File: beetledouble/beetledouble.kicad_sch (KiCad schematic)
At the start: 27 parts, among them J1 power in, J2 rxin, J6 prog connector, U1 78L12G-AB3-R, U2 DD4012SB, U3 ATtiny1614-SS

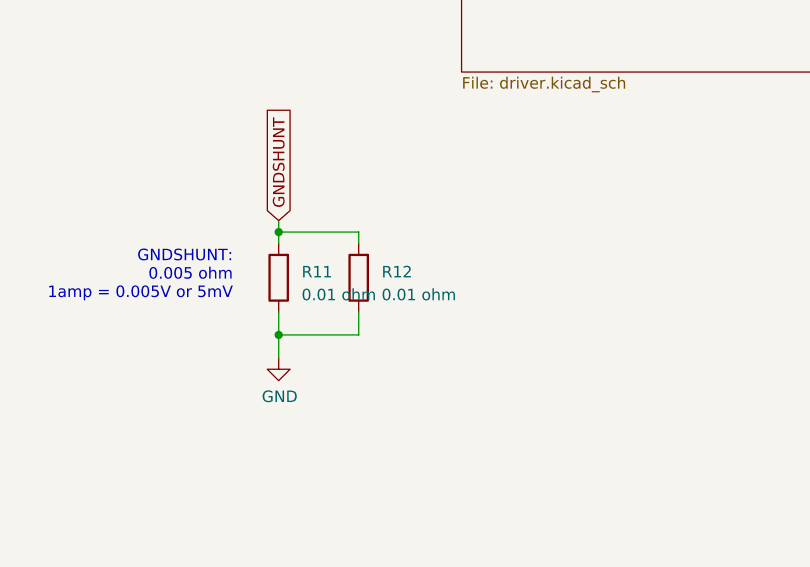
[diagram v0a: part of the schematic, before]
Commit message: Beetle double driver update with differen fets
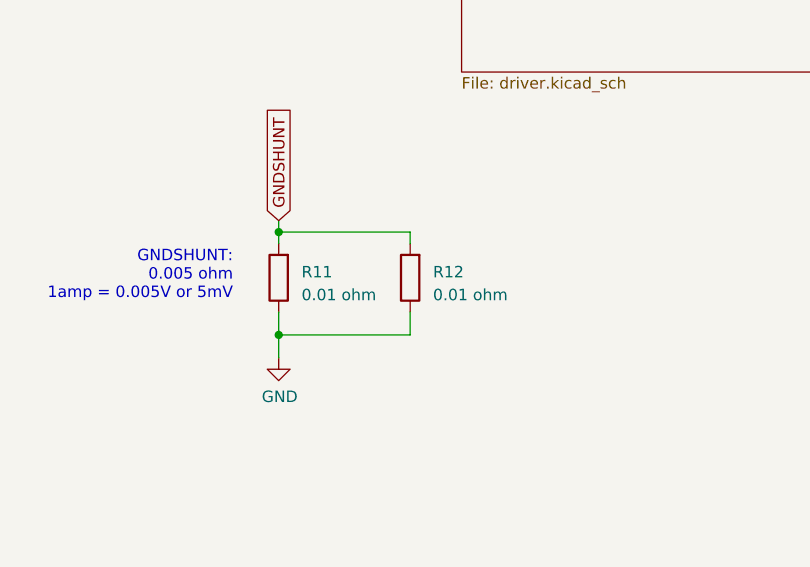
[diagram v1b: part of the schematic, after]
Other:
- moved on the sheet: R12
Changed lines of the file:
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@@
     (stroke (width 0) (type solid) (color 0 0 0 0))
   )
-  (wire (pts (xy 195.58 138.43) (xy 204.47 138.43))
+  (wire (pts (xy 195.58 138.43) (xy 210.185 138.43))
     (stroke (width 0) (type solid) (color 0 0 0 0))
   )
@@
     (stroke (width 0) (type solid) (color 0 0 0 0))
   )
-  (wire (pts (xy 204.47 138.43) (xy 204.47 139.7))
-    (stroke (width 0) (type solid) (color 0 0 0 0))
-  )
-  (wire (pts (xy 204.47 147.32) (xy 204.47 149.86))
-    (stroke (width 0) (type solid) (color 0 0 0 0))
-  )
-  (wire (pts (xy 204.47 149.86) (xy 195.58 149.86))
+  (wire (pts (xy 210.185 138.43) (xy 210.185 139.7))
+    (stroke (width 0) (type solid) (color 0 0 0 0))
+  )
+  (wire (pts (xy 210.185 147.32) (xy 210.185 149.86))
+    (stroke (width 0) (type solid) (color 0 0 0 0))
+  )
+  (wire (pts (xy 210.185 149.86) (xy 195.58 149.86))
     (stroke (width 0) (type solid) (color 0 0 0 0))
   )
@@
     (pin "2")
   )
-  (symbol (lib_id "Device:R") (at 204.47 143.51 180) (unit 1)
-    (in_bom yes) (on_board yes) (fields_autoplaced)
-    (property "Reference" "R12" (id 0) (at 207.01 142.8749 0)
+  (symbol (lib_id "Device:R") (at 210.185 143.51 180) (unit 1)
+    (in_bom yes) (on_board yes) (fields_autoplaced)
+    (property "Reference" "R12" (id 0) (at 212.725 142.8749 0)
       (effects (font (size 1.27 1.27)) (justify right))
     )
-    (property "Value" "0.01 ohm" (id 1) (at 207.01 145.4149 0)
+    (property "Value" "0.01 ohm" (id 1) (at 212.725 145.4149 0)
       (effects (font (size 1.27 1.27)) (justify right))
     )
-    (property "Footprint" "Resistor_SMD:R_2512_6332Metric_Pad1.40x3.35mm_HandSolder" (id 2) (at 206.248 143.51 90)
-      (effects (font (size 1.27 1.27)) hide)
-    )
-    (property "Datasheet" "~" (id 3) (at 204.47 143.51 0)
+    (property "Footprint" "Resistor_SMD:R_2512_6332Metric_Pad1.40x3.35mm_HandSolder" (id 2) (at 211.963 143.51 90)
+      (effects (font (size 1.27 1.27)) hide)
+    )
+    (property "Datasheet" "~" (id 3) (at 210.185 143.51 0)
       (effects (font (size 1.27 1.27)) hide)
     )
@@
       (reference "J4") (unit 1) (value "motor_out") (footprint "Connector_Wire:SolderWire-0.75sqmm_1x02_P4.8mm_D1.25mm_OD2.3mm")
     )
-    (path "/04625774-148a-4b57-bc94-9367edc01ebb/b1a06d2a-a007-41d4-9e0c-37fd31a792da"
-      (reference "Q1") (unit 1) (value "IRF8313PBF ") (footprint "Package_SO:SOIC-8_3.9x4.9mm_P1.27mm")
-    )
-    (path "/04625774-148a-4b57-bc94-9367edc01ebb/453e55ff-63c7-4e45-b1a7-07e090e6dab9"
-      (reference "Q1") (unit 2) (value "IRF8313PBF ") (footprint "Package_SO:SOIC-8_3.9x4.9mm_P1.27mm")
-    )
-    (path "/04625774-148a-4b57-bc94-9367edc01ebb/3e33f540-466e-4b3e-a64f-d1be0667f819"
-      (reference "Q2") (unit 1) (value "IRF8313PBF ") (footprint "Package_SO:SOIC-8_3.9x4.9mm_P1.27mm")
-    )
-    (path "/04625774-148a-4b57-bc94-9367edc01ebb/f58403f9-1add-43f1-814c-ff493d5d1e52"
-      (reference "Q2") (unit 2) (value "IRF8313PBF ") (footprint "Package_SO:SOIC-8_3.9x4.9mm_P1.27mm")
+    (path "/04625774-148a-4b57-bc94-9367edc01ebb/91401f80-e11e-4dcd-8127-cf1209ae9c95"
+      (reference "Q1") (unit 1) (value "IPG20N04S4-12") (footprint "beetledouble:Infineon-PG-TDSON")
+    )
+    (path "/04625774-148a-4b57-bc94-9367edc01ebb/78f7d384-c1e8-43be-9cf5-ea0b8e5ee852"
+      (reference "Q1") (unit 2) (value "IPG20N04S4-12") (footprint "beetledouble:Infineon-PG-TDSON")
+    )
+    (path "/04625774-148a-4b57-bc94-9367edc01ebb/e735ae3b-e647-4157-bf24-522fcab1aa8b"
+      (reference "Q2") (unit 1) (value "IPG20N04S4-12") (footprint "beetledouble:Infineon-PG-TDSON")
+    )
+    (path "/04625774-148a-4b57-bc94-9367edc01ebb/a45d94ed-e4aa-467a-8892-f6d35332ba60"
+      (reference "Q2") (unit 2) (value "IPG20N04S4-12") (footprint "beetledouble:Infineon-PG-TDSON")
     )
     (path "/04625774-148a-4b57-bc94-9367edc01ebb/fad7411d-71dd-41a2-9e10-172d90ee0b89"
@@
       (reference "J5") (unit 1) (value "motor_out") (footprint "Connector_Wire:SolderWire-0.75sqmm_1x02_P4.8mm_D1.25mm_OD2.3mm")
     )
-    (path "/4bcd2397-838c-4768-a766-b8196d1dcd9f/b1a06d2a-a007-41d4-9e0c-37fd31a792da"
-      (reference "Q3") (unit 1) (value "IRF8313PBF ") (footprint "Package_SO:SOIC-8_3.9x4.9mm_P1.27mm")
-    )
-    (path "/4bcd2397-838c-4768-a766-b8196d1dcd9f/453e55ff-63c7-4e45-b1a7-07e090e6dab9"
-      (reference "Q3") (unit 2) (value "IRF8313PBF ") (footprint "Package_SO:SOIC-8_3.9x4.9mm_P1.27mm")
-    )
-    (path "/4bcd2397-838c-4768-a766-b8196d1dcd9f/3e33f540-466e-4b3e-a64f-d1be0667f819"
-      (reference "Q4") (unit 1) (value "IRF8313PBF ") (footprint "Package_SO:SOIC-8_3.9x4.9mm_P1.27mm")
-    )
-    (path "/4bcd2397-838c-4768-a766-b8196d1dcd9f/f58403f9-1add-43f1-814c-ff493d5d1e52"
-      (reference "Q4") (unit 2) (value "IRF8313PBF ") (footprint "Package_SO:SOIC-8_3.9x4.9mm_P1.27mm")
+    (path "/4bcd2397-838c-4768-a766-b8196d1dcd9f/91401f80-e11e-4dcd-8127-cf1209ae9c95"
+      (reference "Q3") (unit 1) (value "IPG20N04S4-12") (footprint "beetledouble:Infineon-PG-TDSON")
+    )
+    (path "/4bcd2397-838c-4768-a766-b8196d1dcd9f/78f7d384-c1e8-43be-9cf5-ea0b8e5ee852"
+      (reference "Q3") (unit 2) (value "IPG20N04S4-12") (footprint "beetledouble:Infineon-PG-TDSON")
+    )
+    (path "/4bcd2397-838c-4768-a766-b8196d1dcd9f/e735ae3b-e647-4157-bf24-522fcab1aa8b"
+      (reference "Q4") (unit 1) (value "IPG20N04S4-12") (footprint "beetledouble:Infineon-PG-TDSON")
+    )
+    (path "/4bcd2397-838c-4768-a766-b8196d1dcd9f/a45d94ed-e4aa-467a-8892-f6d35332ba60"
+      (reference "Q4") (unit 2) (value "IPG20N04S4-12") (footprint "beetledouble:Infineon-PG-TDSON")
     )
     (path "/4bcd2397-838c-4768-a766-b8196d1dcd9f/fad7411d-71dd-41a2-9e10-172d90ee0b89"

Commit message: beetledouble esc wip
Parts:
- added C10: 2.2uF, Capacitor_SMD:C_0603_1608Metric, symbol Device:C
- J1: value power in -> XT30PW-M
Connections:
- net GND: now also C10.2
- net ISENSE: now also C10.1
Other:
- moved on the sheet: R13
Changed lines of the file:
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@@
   (junction (at 71.755 99.695) (diameter 0.9144) (color 0 0 0 0))
   (junction (at 76.835 99.695) (diameter 0.9144) (color 0 0 0 0))
+  (junction (at 119.38 78.74) (diameter 0.9144) (color 0 0 0 0))
   (junction (at 137.16 189.23) (diameter 0.9144) (color 0 0 0 0))
   (junction (at 152.4 60.96) (diameter 0.9144) (color 0 0 0 0))
@@
     (stroke (width 0) (type solid) (color 0 0 0 0))
   )
-  (wire (pts (xy 120.65 78.74) (xy 120.65 81.28))
+  (wire (pts (xy 111.76 78.74) (xy 119.38 78.74))
+    (stroke (width 0) (type solid) (color 0 0 0 0))
+  )
+  (wire (pts (xy 119.38 78.74) (xy 119.38 83.82))
+    (stroke (width 0) (type solid) (color 0 0 0 0))
+  )
+  (wire (pts (xy 119.38 78.74) (xy 137.16 78.74))
     (stroke (width 0) (type solid) (color 0 0 0 0))
   )
@@
   )
   (wire (pts (xy 134.62 60.96) (xy 152.4 60.96))
-    (stroke (width 0) (type solid) (color 0 0 0 0))
-  )
-  (wire (pts (xy 137.16 78.74) (xy 120.65 78.74))
     (stroke (width 0) (type solid) (color 0 0 0 0))
   )
@@
     )
   )
-  (global_label "GNDSHUNT" (shape input) (at 120.65 88.9 270)
+  (global_label "GNDSHUNT" (shape input) (at 111.76 86.36 270)
     (effects (font (size 1.27 1.27)) (justify right))
-    (property "Intersheet References" "${INTERSHEET_REFS}" (id 0) (at 120.5706 102.8761 90)
+    (property "Intersheet References" "${INTERSHEET_REFS}" (id 0) (at 111.6806 100.3361 90)
       (effects (font (size 1.27 1.27)) (justify right) hide)
     )
@@
     (pin "1")
   )
+  (symbol (lib_id "power:GND") (at 119.38 91.44 0) (unit 1)
+    (in_bom yes) (on_board yes)
+    (property "Reference" "#PWR0102" (id 0) (at 119.38 97.79 0)
+      (effects (font (size 1.27 1.27)) hide)
+    )
+    (property "Value" "GND" (id 1) (at 119.4943 95.7644 0))
+    (property "Footprint" "" (id 2) (at 119.38 91.44 0)
+      (effects (font (size 1.27 1.27)) hide)
+    )
+    (property "Datasheet" "" (id 3) (at 119.38 91.44 0)
+      (effects (font (size 1.27 1.27)) hide)
+    )
+    (pin "1")
+  )
   (symbol (lib_id "power:GND") (at 134.62 68.58 0) (unit 1)
     (in_bom yes) (on_board yes)
@@
     (pin "2")
   )
-  (symbol (lib_id "Device:R") (at 120.65 85.09 180) (unit 1)
-    (in_bom yes) (on_board yes)
-    (property "Reference" "R13" (id 0) (at 115.4238 85.09 90))
-    (property "Value" "1k" (id 1) (at 117.7225 85.09 90))
-    (property "Footprint" "Resistor_SMD:R_0603_1608Metric" (id 2) (at 122.428 85.09 90)
-      (effects (font (size 1.27 1.27)) hide)
-    )
-    (property "Datasheet" "~" (id 3) (at 120.65 85.09 0)
+  (symbol (lib_id "Device:R") (at 111.76 82.55 180) (unit 1)
+    (in_bom yes) (on_board yes)
+    (property "Reference" "R13" (id 0) (at 106.5338 82.55 90))
+    (property "Value" "1k" (id 1) (at 108.8325 82.55 90))
+    (property "Footprint" "Resistor_SMD:R_0603_1608Metric" (id 2) (at 113.538 82.55 90)
+      (effects (font (size 1.27 1.27)) hide)
+    )
+    (property "Datasheet" "~" (id 3) (at 111.76 82.55 0)
       (effects (font (size 1.27 1.27)) hide)
     )
@@
     (in_bom yes) (on_board yes)
     (property "Reference" "J1" (id 0) (at 25.5524 55.88 0))
-    (property "Value" "power in" (id 1) (at 24.2824 53.34 0))
+    (property "Value" "XT30PW-M" (id 1) (at 24.2824 53.34 0))
     (property "Footprint" "beetledouble:beetlepower" (id 2) (at 22.86 62.23 0)
       (effects (font (size 1.27 1.27)) hide)
@@
     )
     (property "LCSC" "C50254" (id 4) (at 71.755 103.505 0)
+      (effects (font (size 1.27 1.27)) hide)
+    )
+    (pin "1")
+    (pin "2")
+  )
+  (symbol (lib_id "Device:C") (at 119.38 87.63 0) (unit 1)
+    (in_bom yes) (on_board yes)
+    (property "Reference" "C10" (id 0) (at 122.301 86.481 0)
+      (effects (font (size 1.27 1.27)) (justify left))
+    )
+    (property "Value" "2.2uF" (id 1) (at 122.3011 88.7793 0)
+      (effects (font (size 1.27 1.27)) (justify left))
+    )
+    (property "Footprint" "Capacitor_SMD:C_0603_1608Metric" (id 2) (at 120.3452 91.44 0)
+      (effects (font (size 1.27 1.27)) hide)
+    )
+    (property "Datasheet" "~" (id 3) (at 119.38 87.63 0)
+      (effects (font (size 1.27 1.27)) hide)
+    )
+    (property "LCSC" "" (id 4) (at 119.38 87.63 0)
       (effects (font (size 1.27 1.27)) hide)
     )
@@
       (reference "#PWR0101") (unit 1) (value "GND") (footprint "")
     )
+    (path "/3a8b150a-c300-43cd-8e05-40b55ad8dd46"
+      (reference "#PWR0102") (unit 1) (value "GND") (footprint "")
+    )
     (path "/3d5e6458-1bc6-4cb1-8b72-23ca99e73989"
       (reference "#PWR0103") (unit 1) (value "+5V") (footprint "")
@@
       (reference "C9") (unit 1) (value "0.1uF") (footprint "Capacitor_SMD:C_0603_1608Metric")
     )
+    (path "/ec931dfe-fcd6-43aa-a942-f11aa5bf6441"
+      (reference "C10") (unit 1) (value "2.2uF") (footprint "Capacitor_SMD:C_0603_1608Metric")
+    )
     (path "/c473e51e-eda3-4e25-b100-c0ce34b1e3be"
       (reference "D1") (unit 1) (value "LED") (footprint "LED_SMD:LED_0603_1608Metric_Pad1.05x0.95mm_HandSolder")
@@
     )
     (path "/b70e717b-9e3e-42dc-96e9-65039080dd01"
-      (reference "J1") (unit 1) (value "power in") (footprint "beetledouble:beetlepower")
+      (reference "J1") (unit 1) (value "XT30PW-M") (footprint "beetledouble:beetlepower")
     )
     (path "/259582c8-52ac-48ed-9e5f-c74948d79057"

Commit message: Beetle esc
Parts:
- C10: value 2.2uF -> 2.2uF 50V; LCSC (none) -> C50254
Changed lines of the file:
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@@
       (effects (font (size 1.27 1.27)) (justify left))
     )
-    (property "Value" "2.2uF" (id 1) (at 122.3011 88.7793 0)
+    (property "Value" "2.2uF 50V" (id 1) (at 122.3011 88.7793 0)
       (effects (font (size 1.27 1.27)) (justify left))
     )
@@
       (effects (font (size 1.27 1.27)) hide)
     )
-    (property "LCSC" "" (id 4) (at 119.38 87.63 0)
+    (property "LCSC" "C50254" (id 4) (at 119.38 87.63 0)
       (effects (font (size 1.27 1.27)) hide)
     )
@@
     )
     (path "/ec931dfe-fcd6-43aa-a942-f11aa5bf6441"
-      (reference "C10") (unit 1) (value "2.2uF") (footprint "Capacitor_SMD:C_0603_1608Metric")
+      (reference "C10") (unit 1) (value "2.2uF 50V") (footprint "Capacitor_SMD:C_0603_1608Metric")
     )
     (path "/c473e51e-eda3-4e25-b100-c0ce34b1e3be"
@@
       (reference "#PWR09") (unit 1) (value "GND") (footprint "")
     )
+    (path "/04625774-148a-4b57-bc94-9367edc01ebb/349a753b-3547-4ca7-ac39-04fbb7832ae1"
+      (reference "C3") (unit 1) (value "2.2uF 50V") (footprint "Capacitor_SMD:C_0603_1608Metric")
+    )
     (path "/04625774-148a-4b57-bc94-9367edc01ebb/88333258-cec2-4c47-95fd-16fbcefc9469"
-      (reference "C3") (unit 1) (value "2.2uF 50V") (footprint "Capacitor_SMD:C_0603_1608Metric")
-    )
-    (path "/04625774-148a-4b57-bc94-9367edc01ebb/349a753b-3547-4ca7-ac39-04fbb7832ae1"
       (reference "C4") (unit 1) (value "2.2uF 50V") (footprint "Capacitor_SMD:C_0603_1608Metric")
+    )
+    (path "/04625774-148a-4b57-bc94-9367edc01ebb/e0439b6c-59c5-4831-b158-7336fb8aeef6"
+      (reference "D3") (unit 1) (value "B5819W") (footprint "Diode_SMD:D_SOD-123")
+    )
+    (path "/04625774-148a-4b57-bc94-9367edc01ebb/e793d2f4-d15d-4c68-aa28-2d98997ea5fe"
+      (reference "D4") (unit 1) (value "B5819W") (footprint "Diode_SMD:D_SOD-123")
     )
     (path "/04625774-148a-4b57-bc94-9367edc01ebb/8550bf63-6bc2-479c-bddc-082389ddbc28"
@@
     )
     (path "/04625774-148a-4b57-bc94-9367edc01ebb/91401f80-e11e-4dcd-8127-cf1209ae9c95"
-      (reference "Q1") (unit 1) (value "IPG20N04S4-12") (footprint "beetledouble:Infineon-PG-TDSON")
+      (reference "Q1") (unit 1) (value "AON6884") (footprint "beetledouble:Infineon-PG-TDSON")
     )
     (path "/04625774-148a-4b57-bc94-9367edc01ebb/78f7d384-c1e8-43be-9cf5-ea0b8e5ee852"
-      (reference "Q1") (unit 2) (value "IPG20N04S4-12") (footprint "beetledouble:Infineon-PG-TDSON")
+      (reference "Q1") (unit 2) (value "AON6884") (footprint "beetledouble:Infineon-PG-TDSON")
     )
     (path "/04625774-148a-4b57-bc94-9367edc01ebb/e735ae3b-e647-4157-bf24-522fcab1aa8b"
-      (reference "Q2") (unit 1) (value "IPG20N04S4-12") (footprint "beetledouble:Infineon-PG-TDSON")
+      (reference "Q2") (unit 1) (value "AON6884") (footprint "beetledouble:Infineon-PG-TDSON")
     )
     (path "/04625774-148a-4b57-bc94-9367edc01ebb/a45d94ed-e4aa-467a-8892-f6d35332ba60"
-      (reference "Q2") (unit 2) (value "IPG20N04S4-12") (footprint "beetledouble:Infineon-PG-TDSON")
+      (reference "Q2") (unit 2) (value "AON6884") (footprint "beetledouble:Infineon-PG-TDSON")
     )
     (path "/04625774-148a-4b57-bc94-9367edc01ebb/fad7411d-71dd-41a2-9e10-172d90ee0b89"
@@
       (reference "R4") (unit 1) (value "10R") (footprint "Resistor_SMD:R_0603_1608Metric")
     )
-    (path "/04625774-148a-4b57-bc94-9367edc01ebb/95483e26-d500-422a-bbff-b6400f3d51be"
-      (reference "U4") (unit 1) (value "NCP81155MNTXG") (footprint "beetledouble:DFN-8-3x3mm_hand1")
-    )
-    (path "/04625774-148a-4b57-bc94-9367edc01ebb/7e2cc32c-9391-4594-89cf-8d65ae70b10c"
-      (reference "U5") (unit 1) (value "NCP81155MNTXG") (footprint "beetledouble:DFN-8-3x3mm_hand1")
+    (path "/04625774-148a-4b57-bc94-9367edc01ebb/074b7fbd-db44-4cf2-a152-10215821aa61"
+      (reference "U4") (unit 1) (value "ADP3110A") (footprint "beetledouble:DFN-8-3x3mm_hand1")
+    )
+    (path "/04625774-148a-4b57-bc94-9367edc01ebb/9ede5968-a869-4148-88dc-1a510a7e3341"
+      (reference "U5") (unit 1) (value "ADP3110A") (footprint "beetledouble:DFN-8-3x3mm_hand1")
     )
     (path "/4bcd2397-838c-4768-a766-b8196d1dcd9f/5beb08dd-33fb-4b19-bec1-9311e4c1305f"
@@
       (reference "#PWR013") (unit 1) (value "GND") (footprint "")
     )
+    (path "/4bcd2397-838c-4768-a766-b8196d1dcd9f/349a753b-3547-4ca7-ac39-04fbb7832ae1"
+      (reference "C5") (unit 1) (value "2.2uF 50V") (footprint "Capacitor_SMD:C_0603_1608Metric")
+    )
     (path "/4bcd2397-838c-4768-a766-b8196d1dcd9f/88333258-cec2-4c47-95fd-16fbcefc9469"
-      (reference "C5") (unit 1) (value "2.2uF 50V") (footprint "Capacitor_SMD:C_0603_1608Metric")
-    )
-    (path "/4bcd2397-838c-4768-a766-b8196d1dcd9f/349a753b-3547-4ca7-ac39-04fbb7832ae1"
       (reference "C6") (unit 1) (value "2.2uF 50V") (footprint "Capacitor_SMD:C_0603_1608Metric")
+    )
+    (path "/4bcd2397-838c-4768-a766-b8196d1dcd9f/e0439b6c-59c5-4831-b158-7336fb8aeef6"
+      (reference "D5") (unit 1) (value "B5819W") (footprint "Diode_SMD:D_SOD-123")
+    )
+    (path "/4bcd2397-838c-4768-a766-b8196d1dcd9f/e793d2f4-d15d-4c68-aa28-2d98997ea5fe"
+      (reference "D6") (unit 1) (value "B5819W") (footprint "Diode_SMD:D_SOD-123")
     )
     (path "/4bcd2397-838c-4768-a766-b8196d1dcd9f/8550bf63-6bc2-479c-bddc-082389ddbc28"
@@
     )
     (path "/4bcd2397-838c-4768-a766-b8196d1dcd9f/91401f80-e11e-4dcd-8127-cf1209ae9c95"
-      (reference "Q3") (unit 1) (value "IPG20N04S4-12") (footprint "beetledouble:Infineon-PG-TDSON")
+      (reference "Q3") (unit 1) (value "AON6884") (footprint "beetledouble:Infineon-PG-TDSON")
     )
     (path "/4bcd2397-838c-4768-a766-b8196d1dcd9f/78f7d384-c1e8-43be-9cf5-ea0b8e5ee852"
-      (reference "Q3") (unit 2) (value "IPG20N04S4-12") (footprint "beetledouble:Infineon-PG-TDSON")
+      (reference "Q3") (unit 2) (value "AON6884") (footprint "beetledouble:Infineon-PG-TDSON")
     )
     (path "/4bcd2397-838c-4768-a766-b8196d1dcd9f/e735ae3b-e647-4157-bf24-522fcab1aa8b"
-      (reference "Q4") (unit 1) (value "IPG20N04S4-12") (footprint "beetledouble:Infineon-PG-TDSON")
+      (reference "Q4") (unit 1) (value "AON6884") (footprint "beetledouble:Infineon-PG-TDSON")
     )
     (path "/4bcd2397-838c-4768-a766-b8196d1dcd9f/a45d94ed-e4aa-467a-8892-f6d35332ba60"
-      (reference "Q4") (unit 2) (value "IPG20N04S4-12") (footprint "beetledouble:Infineon-PG-TDSON")
+      (reference "Q4") (unit 2) (value "AON6884") (footprint "beetledouble:Infineon-PG-TDSON")
     )
     (path "/4bcd2397-838c-4768-a766-b8196d1dcd9f/fad7411d-71dd-41a2-9e10-172d90ee0b89"
@@
       (reference "R8") (unit 1) (value "10R") (footprint "Resistor_SMD:R_0603_1608Metric")
     )
-    (path "/4bcd2397-838c-4768-a766-b8196d1dcd9f/95483e26-d500-422a-bbff-b6400f3d51be"
-      (reference "U6") (unit 1) (value "NCP81155MNTXG") (footprint "beetledouble:DFN-8-3x3mm_hand1")
-    )
-    (path "/4bcd2397-838c-4768-a766-b8196d1dcd9f/7e2cc32c-9391-4594-89cf-8d65ae70b10c"
-      (reference "U7") (unit 1) (value "NCP81155MNTXG") (footprint "beetledouble:DFN-8-3x3mm_hand1")
-    )
-  )
+    (path "/4bcd2397-838c-4768-a766-b8196d1dcd9f/074b7fbd-db44-4cf2-a152-10215821aa61"
+      (reference "U6") (unit 1) (value "ADP3110A") (footprint "beetledouble:DFN-8-3x3mm_hand1")
+    )
+    (path "/4bcd2397-838c-4768-a766-b8196d1dcd9f/9ede5968-a869-4148-88dc-1a510a7e3341"
+      (reference "U7") (unit 1) (value "ADP3110A") (footprint "beetledouble:DFN-8-3x3mm_hand1")
+    )
+  )

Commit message: fix capcitor lcsc id, change driver chip to NCP81155
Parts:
- C10, C2: LCSC C50254 -> C326557
- C9: LCSC (none) -> C14663
- D1, D2: LCSC (none) -> C2286

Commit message: Updates
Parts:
- added JP1: CONFIG1, Jumper:SolderJumper-2_P1.3mm_Open_TrianglePad1.0x1.5mm, symbol Jumper:SolderJumper_2_Open
- C10, C2: LCSC C326557 -> C162273
- R10, R13, R14, R15, R9: LCSC (none) -> C21190
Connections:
- net GND: now also JP1.1 (A)
- net RXDEBUG: no longer names the net of J6.2 (Pin_2)
- net RXDEBUG: no longer U3.12 (PA2)
- new net CONFIG1: JP1.2 (B), U3.12 (PA2)
- no-connect marks 5 -> 6
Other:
- note added: "Can also use a PTH TO220 5v Reg e,g, LM7805"
- note added: "Config jumper"
- note added: "Programming connector"
- note added: "Short to disable mixing"
- moved on the sheet: J6

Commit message: Updates
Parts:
- R11, R12: LCSC (none) -> C146895
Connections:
- net PWMIN_1: now also U3.6 (PB3); no longer U3.13 (PA3)
- net PWMIN_2: now also U3.13 (PA3); no longer U3.6 (PB3)
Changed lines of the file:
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@@
     )
   )
-  (global_label "PWMIN_2" (shape input) (at 137.16 81.28 180) (fields_autoplaced)
+  (global_label "PWMIN_1" (shape input) (at 137.16 81.28 180) (fields_autoplaced)
     (effects (font (size 1.27 1.27)) (justify right))
     (property "Intersheet References" "${INTERSHEET_REFS}" (id 0) (at 126.4617 81.3594 0)
@@
     )
   )
-  (global_label "PWMIN_1" (shape input) (at 167.64 81.28 0) (fields_autoplaced)
+  (global_label "PWMIN_2" (shape input) (at 167.64 81.28 0) (fields_autoplaced)
     (effects (font (size 1.27 1.27)) (justify left))
     (property "Intersheet References" "${INTERSHEET_REFS}" (id 0) (at 178.3383 81.2006 0)
@@
       (effects (font (size 1.27 1.27)) hide)
     )
+    (property "LCSC" "C146895" (id 4) (at 195.58 143.51 0)
+      (effects (font (size 1.27 1.27)) hide)
+    )
     (pin "1")
     (pin "2")
@@
       (effects (font (size 1.27 1.27)) hide)
     )
+    (property "LCSC" "C146895" (id 4) (at 210.185 143.51 0)
+      (effects (font (size 1.27 1.27)) hide)
+    )
